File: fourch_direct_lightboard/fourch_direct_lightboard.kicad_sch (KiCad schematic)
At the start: 73 parts, among them J1 Conn_01x01_Pin, J10 Conn_01x01_Pin, J11 Conn_01x01_Pin, J12 Conn_01x01_Pin, J2 Conn_01x01_Pin, J3 Conn_01x01_Pin, J4 Conn_01x01_Pin, J5 Conn_01x01_Pin, J6 Conn_01x01_Pin, J7 Conn_01x01_Pin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

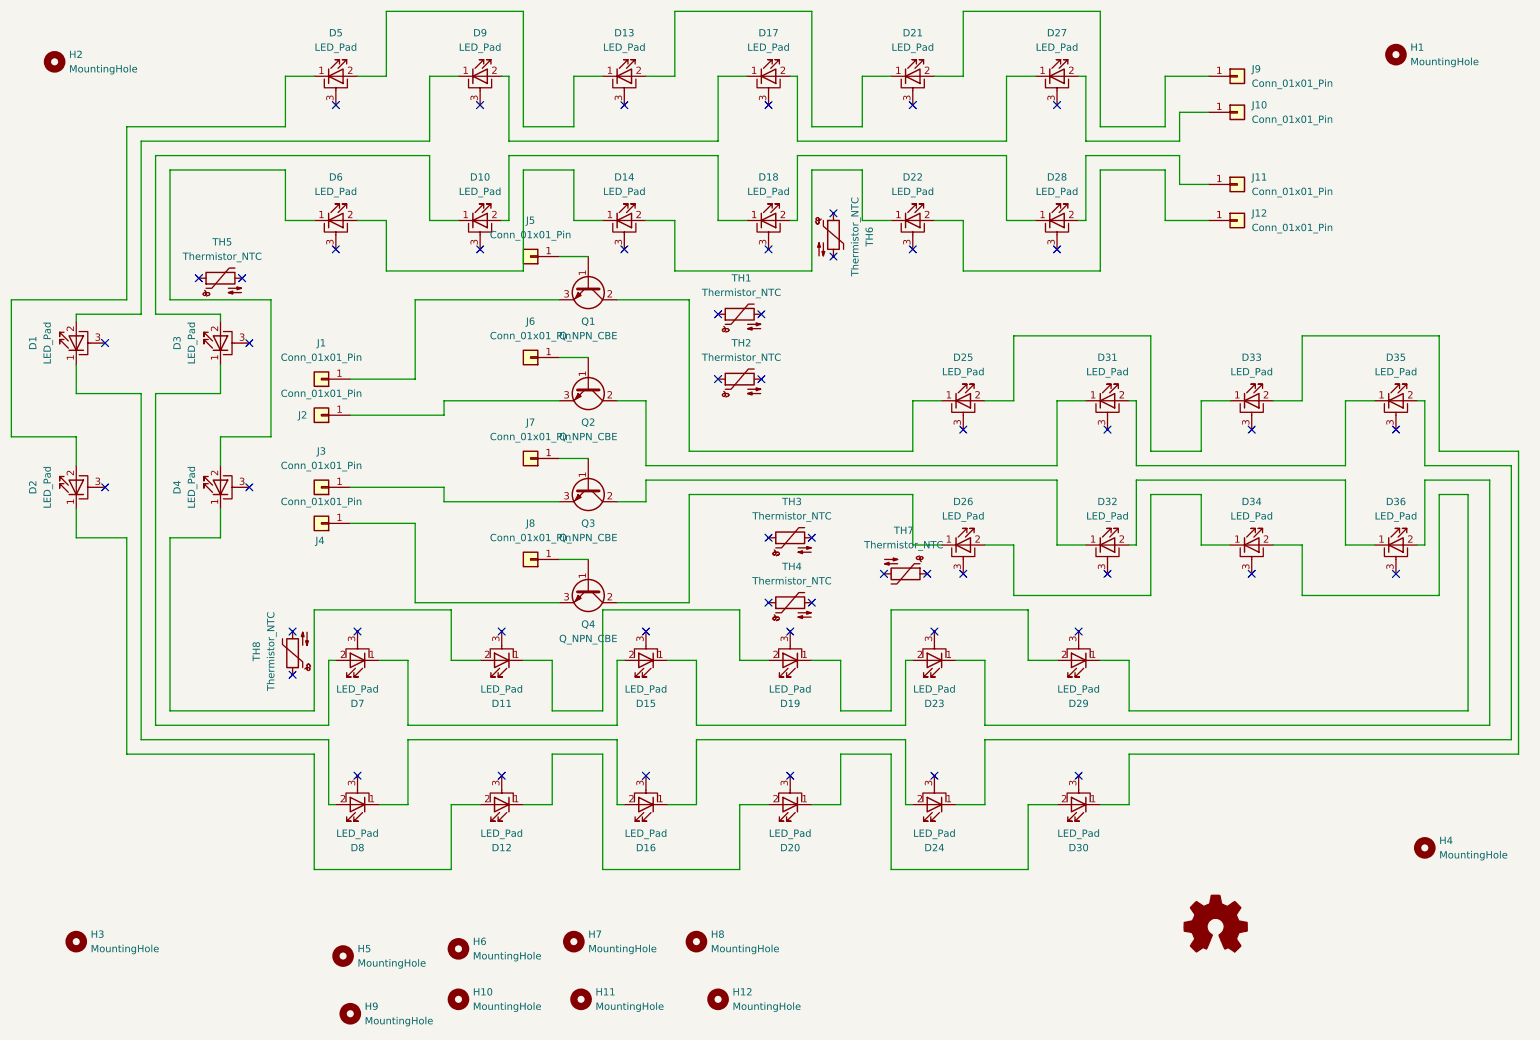
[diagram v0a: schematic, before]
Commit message: rev up fourch lights, add distroboard
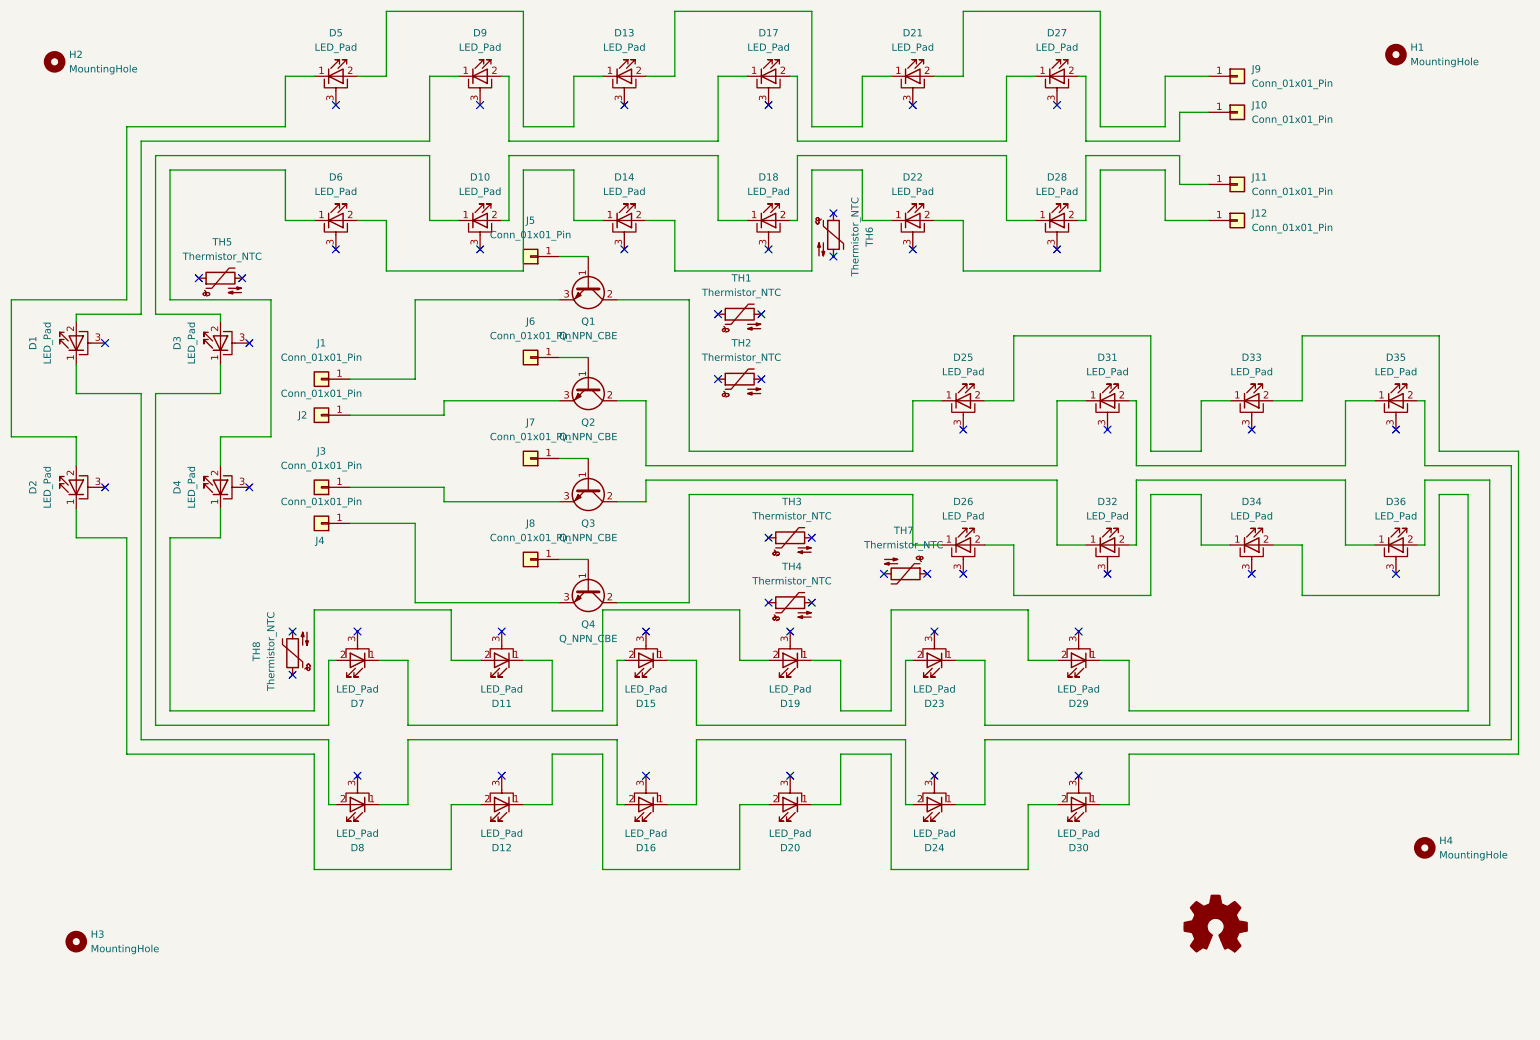
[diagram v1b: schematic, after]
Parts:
- removed H10, H11, H12, H5, H6, H7, H8, H9: MountingHole, custom:MountingHole_4.2mm, symbol Mechanical:MountingHole
- H1, H2, H3, H4: footprint custom:MountingHole_3.0mm -> custom:MountingHole_3.50mm

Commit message: minor touchups
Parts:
- J1, J10, J11, J12, J2, J3, J4, J5, J6, J7, J8, J9, TH1, TH2, TH3, TH4, TH5, TH6, TH7, TH8: now not fitted
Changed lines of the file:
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@@
 		(in_bom yes)
 		(on_board yes)
-		(dnp no)
+		(dnp yes)
 		(property "Reference" "J2"
 			(at 69.088 85.09 0)
@@
 		(in_bom yes)
 		(on_board yes)
-		(dnp no)
+		(dnp yes)
 		(fields_autoplaced yes)
 		(property "Reference" "TH5"
@@
 		(in_bom yes)
 		(on_board yes)
-		(dnp no)
+		(dnp yes)
 		(fields_autoplaced yes)
 		(property "Reference" "J9"
@@
 		(in_bom yes)
 		(on_board yes)
-		(dnp no)
+		(dnp yes)
 		(fields_autoplaced yes)
 		(property "Reference" "TH2"
@@
 		(in_bom yes)
 		(on_board yes)
-		(dnp no)
+		(dnp yes)
 		(property "Reference" "J4"
 			(at 72.136 107.188 0)
@@
 		(in_bom yes)
 		(on_board yes)
-		(dnp no)
+		(dnp yes)
 		(fields_autoplaced yes)
 		(property "Reference" "J11"
@@
 		(in_bom yes)
 		(on_board yes)
-		(dnp no)
+		(dnp yes)
 		(fields_autoplaced yes)
 		(property "Reference" "TH6"
@@
 		(in_bom yes)
 		(on_board yes)
-		(dnp no)
+		(dnp yes)
 		(fields_autoplaced yes)
 		(property "Reference" "J10"
@@
 		(in_bom yes)
 		(on_board yes)
-		(dnp no)
+		(dnp yes)
 		(fields_autoplaced yes)
 		(property "Reference" "J5"
@@
 		(in_bom yes)
 		(on_board yes)
-		(dnp no)
+		(dnp yes)
 		(fields_autoplaced yes)
 		(property "Reference" "J1"
@@
 		(in_bom yes)
 		(on_board yes)
-		(dnp no)
+		(dnp yes)
 		(fields_autoplaced yes)
 		(property "Reference" "J7"
@@
 		(in_bom yes)
 		(on_board yes)
-		(dnp no)
+		(dnp yes)
 		(fields_autoplaced yes)
 		(property "Reference" "J8"
@@
 		(in_bom yes)
 		(on_board yes)
-		(dnp no)
+		(dnp yes)
 		(fields_autoplaced yes)
 		(property "Reference" "TH1"
@@
 		(in_bom yes)
 		(on_board yes)
-		(dnp no)
+		(dnp yes)
 		(fields_autoplaced yes)
 		(property "Reference" "J12"
@@
 		(in_bom yes)
 		(on_board yes)
-		(dnp no)
+		(dnp yes)
 		(fields_autoplaced yes)
 		(property "Reference" "TH3"
@@
 		(in_bom yes)
 		(on_board yes)
-		(dnp no)
+		(dnp yes)
 		(fields_autoplaced yes)
 		(property "Reference" "TH7"
@@
 		(in_bom yes)
 		(on_board yes)
-		(dnp no)
+		(dnp yes)
 		(fields_autoplaced yes)
 		(property "Reference" "TH4"
@@
 		(in_bom yes)
 		(on_board yes)
-		(dnp no)
+		(dnp yes)
 		(fields_autoplaced yes)
 		(property "Reference" "J6"
@@
 		(in_bom yes)
 		(on_board yes)
-		(dnp no)
+		(dnp yes)
 		(fields_autoplaced yes)
 		(property "Reference" "J3"
@@
 		(in_bom yes)
 		(on_board yes)
-		(dnp no)
+		(dnp yes)
 		(fields_autoplaced yes)
 		(property "Reference" "TH8"

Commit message: switch opamps to dual flavors, build in on-board TEC current control
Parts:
- Q1, Q2, Q3, Q4: value Q_NPN_CBE -> NSS1C301ET4G; symbol Device:Q_NPN_BCE -> Transistor_BJT:Q_NPN_BCE
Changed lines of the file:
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@@
 	)
 	(symbol
-		(lib_id "Device:Q_NPN_BCE")
+		(lib_id "Transistor_BJT:Q_NPN_BCE")
 		(at 119.38 115.57 270)
 		(unit 1)
@@
 			)
 		)
-		(property "Value" "Q_NPN_CBE"
+		(property "Value" "NSS1C301ET4G"
 			(at 119.38 124.46 90)
 			(effects
@@
 	)
 	(symbol
-		(lib_id "Device:Q_NPN_BCE")
+		(lib_id "Transistor_BJT:Q_NPN_BCE")
 		(at 119.38 80.01 270)
 		(unit 1)
@@
 			)
 		)
-		(property "Value" "Q_NPN_CBE"
+		(property "Value" "NSS1C301ET4G"
 			(at 119.38 88.9 90)
 			(effects
@@
 	)
 	(symbol
-		(lib_id "Device:Q_NPN_BCE")
+		(lib_id "Transistor_BJT:Q_NPN_BCE")
 		(at 119.38 97.79 270)
 		(unit 1)
@@
 			)
 		)
-		(property "Value" "Q_NPN_CBE"
+		(property "Value" "NSS1C301ET4G"
 			(at 119.38 106.68 90)
 			(effects
@@
 	)
 	(symbol
-		(lib_id "Device:Q_NPN_BCE")
+		(lib_id "Transistor_BJT:Q_NPN_BCE")
 		(at 119.38 62.23 270)
 		(unit 1)
@@
 			)
 		)
-		(property "Value" "Q_NPN_CBE"
+		(property "Value" "NSS1C301ET4G"
 			(at 119.38 71.12 90)
 			(effects

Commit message: rev up light
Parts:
- Q1, Q2, Q3, Q4: value NSS1C301ET4G -> MJD44H11T4
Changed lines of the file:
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@@
 			)
 		)
-		(property "Value" "NSS1C301ET4G"
+		(property "Value" "MJD44H11T4"
 			(at 119.38 124.46 90)
 			(effects
@@
 			)
 		)
-		(property "Value" "NSS1C301ET4G"
+		(property "Value" "MJD44H11T4"
 			(at 119.38 88.9 90)
 			(effects
@@
 			)
 		)
-		(property "Value" "NSS1C301ET4G"
+		(property "Value" "MJD44H11T4"
 			(at 119.38 106.68 90)
 			(effects
@@
 			)
 		)
-		(property "Value" "NSS1C301ET4G"
+		(property "Value" "MJD44H11T4"
 			(at 119.38 71.12 90)
 			(effects
